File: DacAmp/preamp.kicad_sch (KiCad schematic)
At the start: 34 parts, among them U3 NE5532, U6 NE5532, U7 NE5532, U8 NE5532

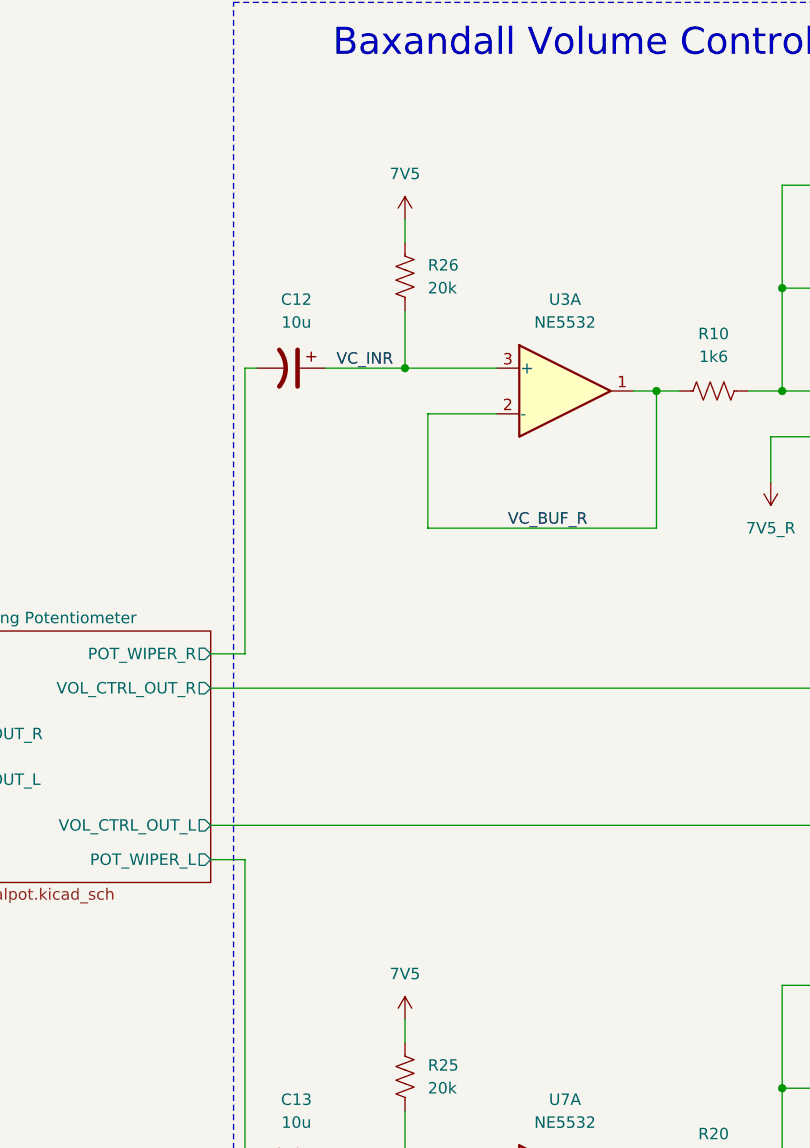
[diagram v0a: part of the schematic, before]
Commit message: add outputs for release 2
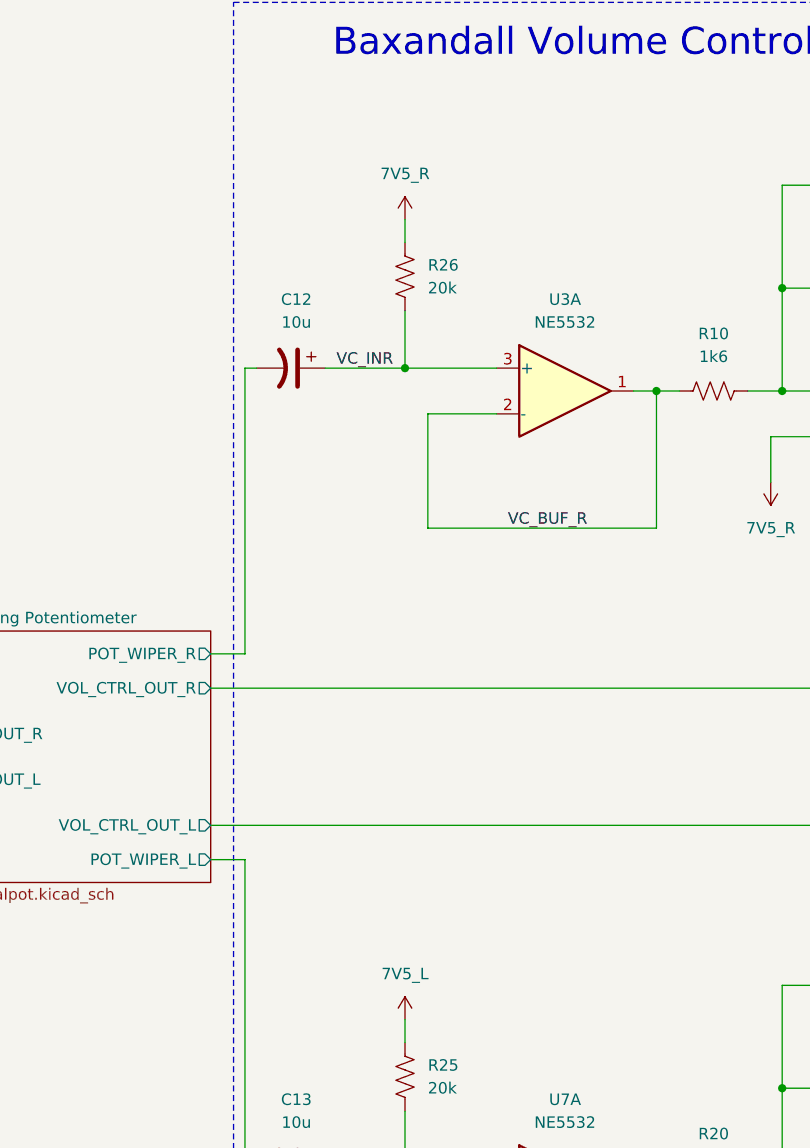
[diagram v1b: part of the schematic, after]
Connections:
- net 7V5_L: now also R25.1
- net 7V5_R: now also R26.1
- removed net 7V5: R25.1, R26.1
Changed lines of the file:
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@@
+	)
+	(symbol
+		(lib_id "power:VCC")
+		(at 228.6 44.45 0)
+		(unit 1)
+		(exclude_from_sim no)
+		(in_bom yes)
+		(on_board yes)
+		(dnp no)
+		(fields_autoplaced yes)
+		(property "Reference" "#PWR027"
+			(at 228.6 48.26 0)
+			(effects
+				(font
+					(size 1.27 1.27)
+				)
+				(hide yes)
+			)
+		)
+		(property "Value" "7V5_R"
+			(at 228.6 39.37 0)
+			(effects
+				(font
+					(size 1.27 1.27)
+				)
+			)
+		)
+		(property "Footprint" ""
+			(at 228.6 44.45 0)
+			(effects
+				(font
+					(size 1.27 1.27)
+				)
+				(hide yes)
+			)
+		)
+		(property "Datasheet" ""
+			(at 228.6 44.45 0)
+			(effects
+				(font
+					(size 1.27 1.27)
+				)
+				(hide yes)
+			)
+		)
+		(property "Description" "Power symbol creates a global label with name \"VCC\""
+			(at 228.6 44.45 0)
+			(effects
+				(font
+					(size 1.27 1.27)
+				)
+				(hide yes)
+			)
+		)
+		(pin "1"
+		)
+		(instances
+			(project "DacAmp"
+				(path "/d6da33f4-6bef-4098-a08b-0ea38da216b8/765aa114-40bf-4fb7-ad02-1003eccfadc3"
+					(reference "#PWR027")
+					(unit 1)
+				)
+			)
+		)
 	)
 	(symbol
@@
 	)
 	(symbol
-		(lib_id "power:VCC")
-		(at 228.6 44.45 0)
-		(unit 1)
-		(exclude_from_sim no)
-		(in_bom yes)
-		(on_board yes)
-		(dnp no)
-		(fields_autoplaced yes)
-		(property "Reference" "#PWR029"
-			(at 228.6 48.26 0)
-			(effects
-				(font
-					(size 1.27 1.27)
-				)
-				(hide yes)
-			)
-		)
-		(property "Value" "7V5"
-			(at 228.6 39.37 0)
-			(effects
-				(font
-					(size 1.27 1.27)
-				)
-			)
-		)
-		(property "Footprint" ""
-			(at 228.6 44.45 0)
-			(effects
-				(font
-					(size 1.27 1.27)
-				)
-				(hide yes)
-			)
-		)
-		(property "Datasheet" ""
-			(at 228.6 44.45 0)
-			(effects
-				(font
-					(size 1.27 1.27)
-				)
-				(hide yes)
-			)
-		)
-		(property "Description" "Power symbol creates a global label with name \"VCC\""
-			(at 228.6 44.45 0)
-			(effects
-				(font
-					(size 1.27 1.27)
-				)
-				(hide yes)
-			)
-		)
-		(pin "1"
-		)
-		(instances
-			(project "DacAmp"
-				(path "/d6da33f4-6bef-4098-a08b-0ea38da216b8/765aa114-40bf-4fb7-ad02-1003eccfadc3"
-					(reference "#PWR029")
-					(unit 1)
-				)
-			)
-		)
-	)
-	(symbol
 		(lib_id "Device:R_US")
 		(at 71.12 133.35 90)
@@
 		(dnp no)
 		(fields_autoplaced yes)
-		(property "Reference" "#PWR027"
+		(property "Reference" "#PWR026"
 			(at 228.6 137.16 0)
 			(effects
@@
 			)
 		)
-		(property "Value" "7V5"
+		(property "Value" "7V5_L"
 			(at 228.6 128.27 0)
 			(effects
@@
 			(project "DacAmp"
 				(path "/d6da33f4-6bef-4098-a08b-0ea38da216b8/765aa114-40bf-4fb7-ad02-1003eccfadc3"
-					(reference "#PWR027")
-					(unit 1)
-				)
+					(reference "#PWR026")
+					(unit 1)
+				)
